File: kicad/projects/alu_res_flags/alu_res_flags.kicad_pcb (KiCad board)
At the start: 2 copper layers, 203.2 x 97.8 mm, 59 parts, among them J1 RES_CRRYBRRW_EQ_IN, J2 Aux_connection, J3 Bus_connection, J4 Control_signal_backplane, J5 ECNZ_OUT, U1 74HCT04, U10 74HCT245, U11 74HCT173, U12 74HCT245, U2 74HCT377, U3 74HCT377, U4 74HCT245, U5 74HCT245, U6 74HCT27, U7 74HCT27, U8 74HCT30, U9 74HCT245

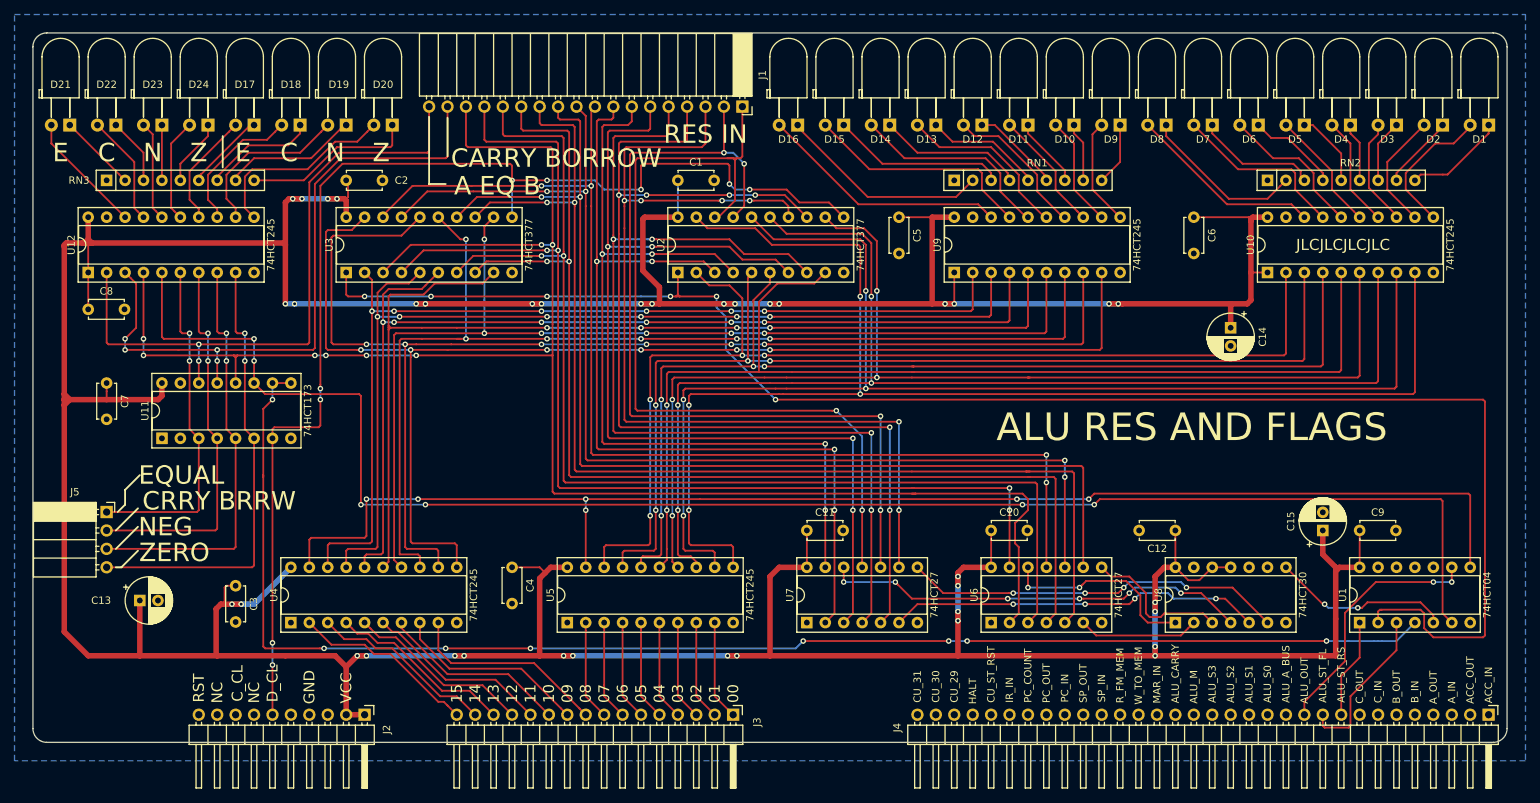
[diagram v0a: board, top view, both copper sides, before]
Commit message: Move kikad libs to sixteen bit location and update projects.
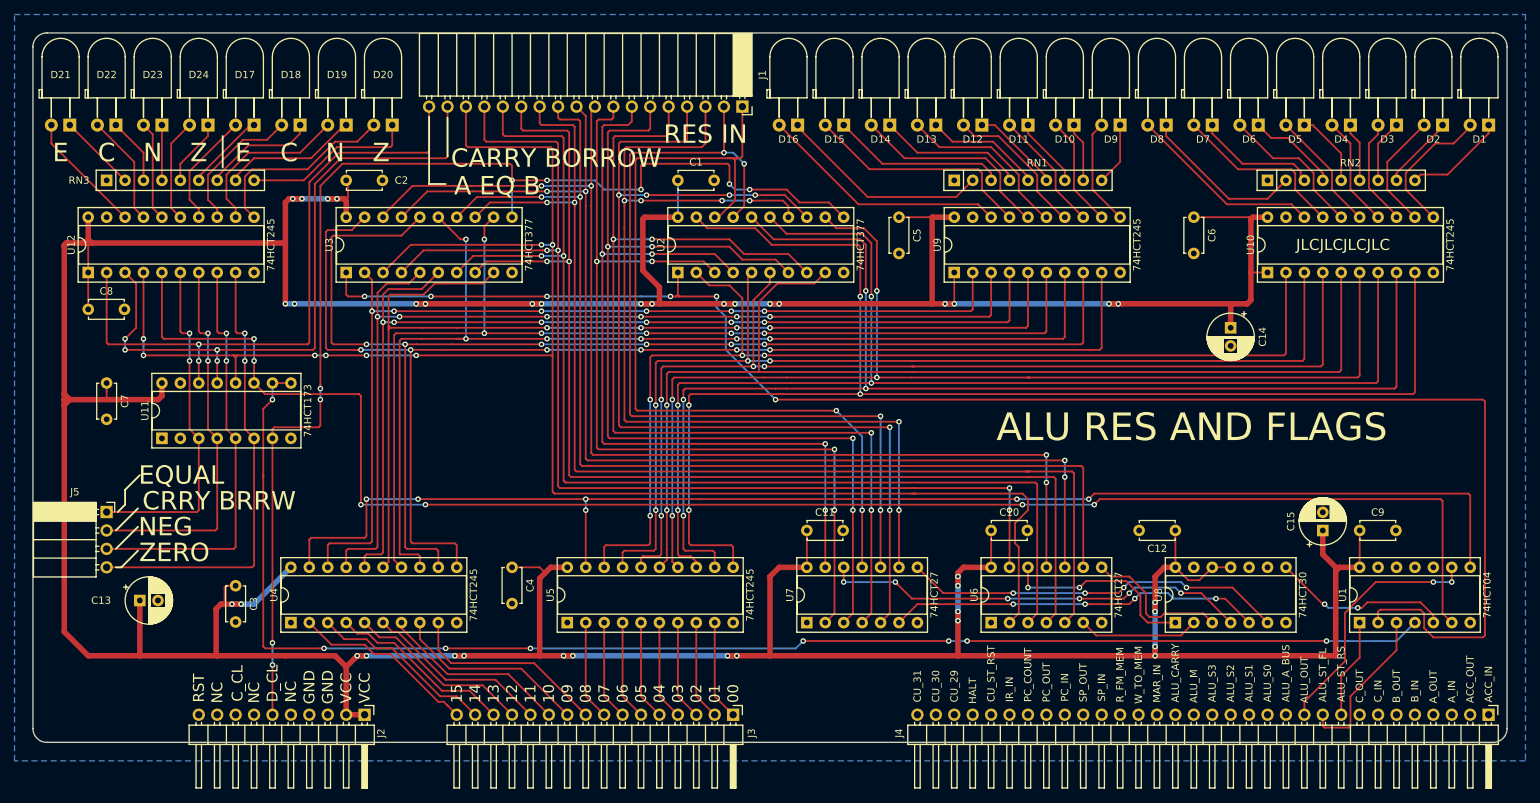
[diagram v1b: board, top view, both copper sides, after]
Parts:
- D1, D10, D11, D12, D13, D14, D15, D16, D17, D18, D19, D2, D20, D21, D22, D23, D24, D3, D4, D5, D6, D7, D8, D9: footprint eight-bit-computer:LED_D5.0mm_Horizontal_O3.81mm_Z3.0mm -> sixteen-bit-computer:LED_D5.0mm_Horizontal_O3.81mm_Z3.0mm
- J2: footprint eight-bit-computer:aux-connection -> sixteen-bit-computer:aux-connection
- J3: footprint eight-bit-computer:bus-connection -> sixteen-bit-computer:bus-connection
- J4: footprint eight-bit-computer:backplane-connector-single-row-annotated -> sixteen-bit-computer:backplane-connector-single-row-annotated

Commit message: Switch to HC series chips and fix some labelling in program counter or register PCB.
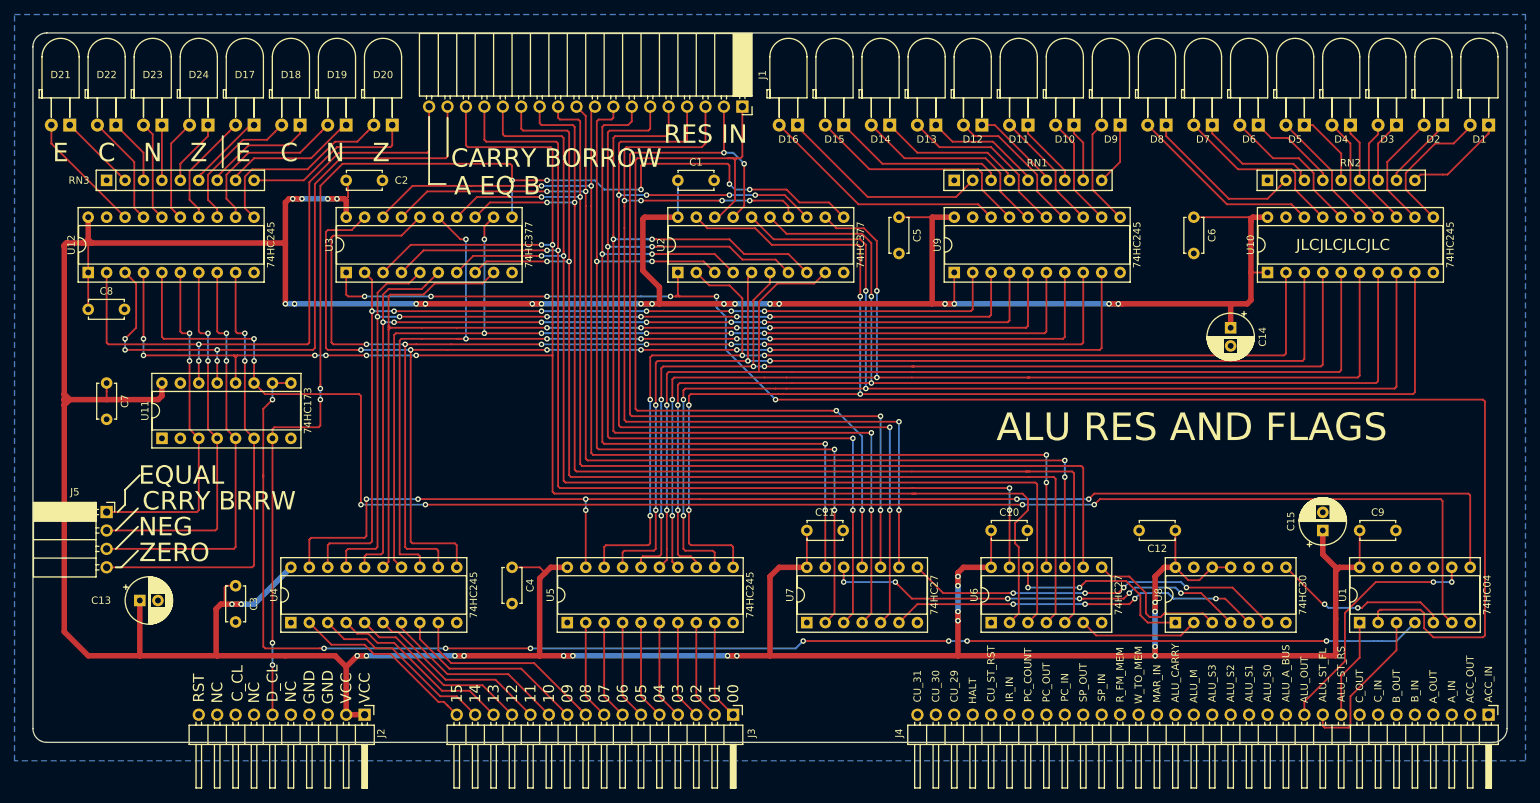
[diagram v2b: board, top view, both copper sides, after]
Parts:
- U1: value 74HCT04 -> 74HC04
- U10, U12, U4, U5, U9: value 74HCT245 -> 74HC245
- U11: value 74HCT173 -> 74HC173
- U2, U3: value 74HCT377 -> 74HC377
- U6, U7: value 74HCT27 -> 74HC27
- U8: value 74HCT30 -> 74HC30
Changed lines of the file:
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@@
       (effects (font (size 1.016 1.016) (thickness 0.1778)))
     )
-    (fp_text value 74HCT30 (at 3.81 17.57 90) (layer F.SilkS)
+    (fp_text value 74HC30 (at 3.81 17.57 90) (layer F.SilkS)
       (effects (font (size 1.016 1.016) (thickness 0.1778)))
     )
@@
       (effects (font (size 1.016 1.016) (thickness 0.1778)))
     )
-    (fp_text value 74HCT245 (at 3.81 25.19 90) (layer F.SilkS)
+    (fp_text value 74HC245 (at 3.81 25.19 90) (layer F.SilkS)
       (effects (font (size 1.016 1.016) (thickness 0.1778)))
     )
@@
       (effects (font (size 1.016 1.016) (thickness 0.1778)))
     )
-    (fp_text value 74HCT173 (at 3.81 20.11 90) (layer F.SilkS)
+    (fp_text value 74HC173 (at 3.81 20.11 90) (layer F.SilkS)
       (effects (font (size 1.016 1.016) (thickness 0.1778)))
     )
@@
       (effects (font (size 1.016 1.016) (thickness 0.1778)))
     )
-    (fp_text value 74HCT245 (at 3.81 25.19 90) (layer F.SilkS)
+    (fp_text value 74HC245 (at 3.81 25.19 90) (layer F.SilkS)
       (effects (font (size 1.016 1.016) (thickness 0.1778)))
     )
@@
       (effects (font (size 1.016 1.016) (thickness 0.1778)))
     )
-    (fp_text value 74HCT245 (at 3.81 25.19 90) (layer F.SilkS)
+    (fp_text value 74HC245 (at 3.81 25.19 90) (layer F.SilkS)
       (effects (font (size 1.016 1.016) (thickness 0.1778)))
     )
@@
       (effects (font (size 1.016 1.016) (thickness 0.1778)))
     )
-    (fp_text value 74HCT27 (at 3.81 17.57 90) (layer F.SilkS)
+    (fp_text value 74HC27 (at 3.81 17.57 90) (layer F.SilkS)
       (effects (font (size 1.016 1.016) (thickness 0.1778)))
     )
@@
       (effects (font (size 1.016 1.016) (thickness 0.1778)))
     )
-    (fp_text value 74HCT27 (at 3.81 17.57 90) (layer F.SilkS)
+    (fp_text value 74HC27 (at 3.81 17.57 90) (layer F.SilkS)
       (effects (font (size 1.016 1.016) (thickness 0.1778)))
     )
@@
       (effects (font (size 1.016 1.016) (thickness 0.1778)))
     )
-    (fp_text value 74HCT245 (at 3.81 25.19 90) (layer F.SilkS)
+    (fp_text value 74HC245 (at 3.81 25.19 90) (layer F.SilkS)
       (effects (font (size 1.016 1.016) (thickness 0.1778)))
     )
@@
       (effects (font (size 1.016 1.016) (thickness 0.1778)))
     )
-    (fp_text value 74HCT245 (at 3.81 25.19 90) (layer F.SilkS)
+    (fp_text value 74HC245 (at 3.81 25.19 90) (layer F.SilkS)
       (effects (font (size 1.016 1.016) (thickness 0.1778)))
     )
@@
       (effects (font (size 1.016 1.016) (thickness 0.1778)))
     )
-    (fp_text value 74HCT377 (at 3.81 25.19 90) (layer F.SilkS)
+    (fp_text value 74HC377 (at 3.81 25.19 90) (layer F.SilkS)
       (effects (font (size 1.016 1.016) (thickness 0.1778)))
     )
@@
       (effects (font (size 1.016 1.016) (thickness 0.1778)))
     )
-    (fp_text value 74HCT377 (at 3.81 25.19 90) (layer F.SilkS)
+    (fp_text value 74HC377 (at 3.81 25.19 90) (layer F.SilkS)
       (effects (font (size 1.016 1.016) (thickness 0.1778)))
     )
@@
       (effects (font (size 1.016 1.016) (thickness 0.1778)))
     )
-    (fp_text value 74HCT04 (at 3.81 17.57 90) (layer F.SilkS)
-      (effects (font (size 1.016 1.016) (thickness 0.1778)))
-    )
+    (fp_text value 74HC04 (at 3.81 17.57 90) (layer F.SilkS)
+      (effects (font (size 1.016 1.016) (thickness 0.1778)))
+    )

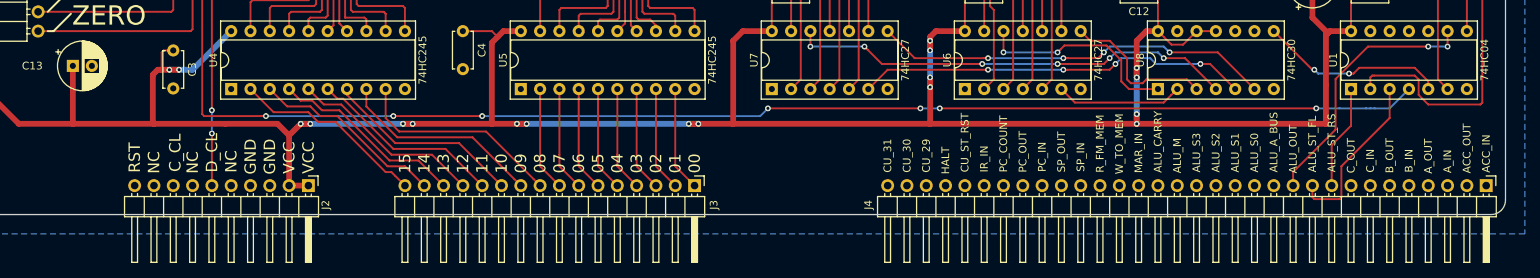
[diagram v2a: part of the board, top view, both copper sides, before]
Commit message: Move alu res flags lower connectors.
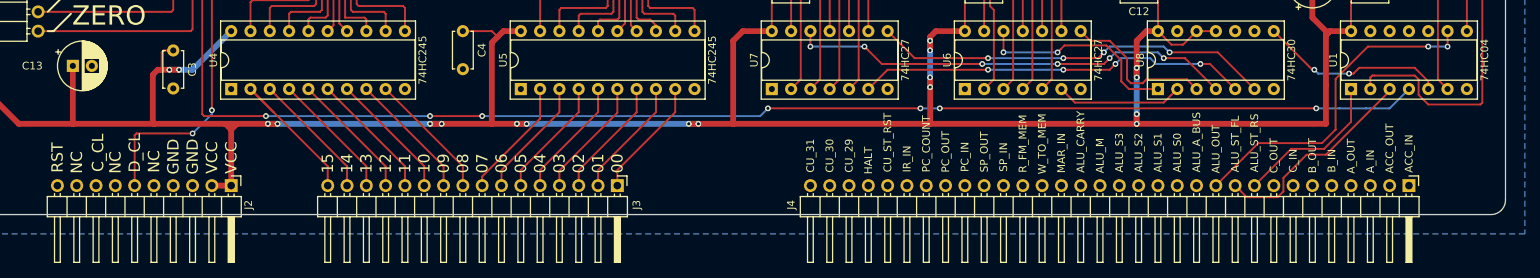
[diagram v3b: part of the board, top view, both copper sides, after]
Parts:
- moved J2 10.2 mm to (86.4, 149.9)
- moved J3 10.2 mm to (137.2, 149.9)
- moved J4 10.2 mm to (241.3, 149.9)
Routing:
- net /BUS_08: track 27.8 -> 16.9 mm
- net /BUS_09: track 26.9 -> 16.9 mm
- net /RES_OUT: track 34.9 -> 44.0 mm
- net /BUS_10: track 26.0 -> 16.9 mm
- net /BUS_14: track 25.6 -> 16.9 mm
- net /BUS_11: track 25.6 -> 16.9 mm
- net /BUS_13: track 25.6 -> 16.9 mm
- net /BUS_12: track 25.6 -> 16.9 mm
- net /CLOCK: track 168.3 -> 176.8 mm
- net /STORE_RES: track 13.8 -> 20.5 mm
- net /STORE_FLAGS: track 22.4 -> 28.0 mm
- net /BUS_15: track 25.6 -> 21.2 mm
- net VCC: track 713.0 -> 715.7 mm
- net /BUS_05: track 13.8 -> 15.9 mm
- net /BUS_07: track 13.8 -> 15.9 mm
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
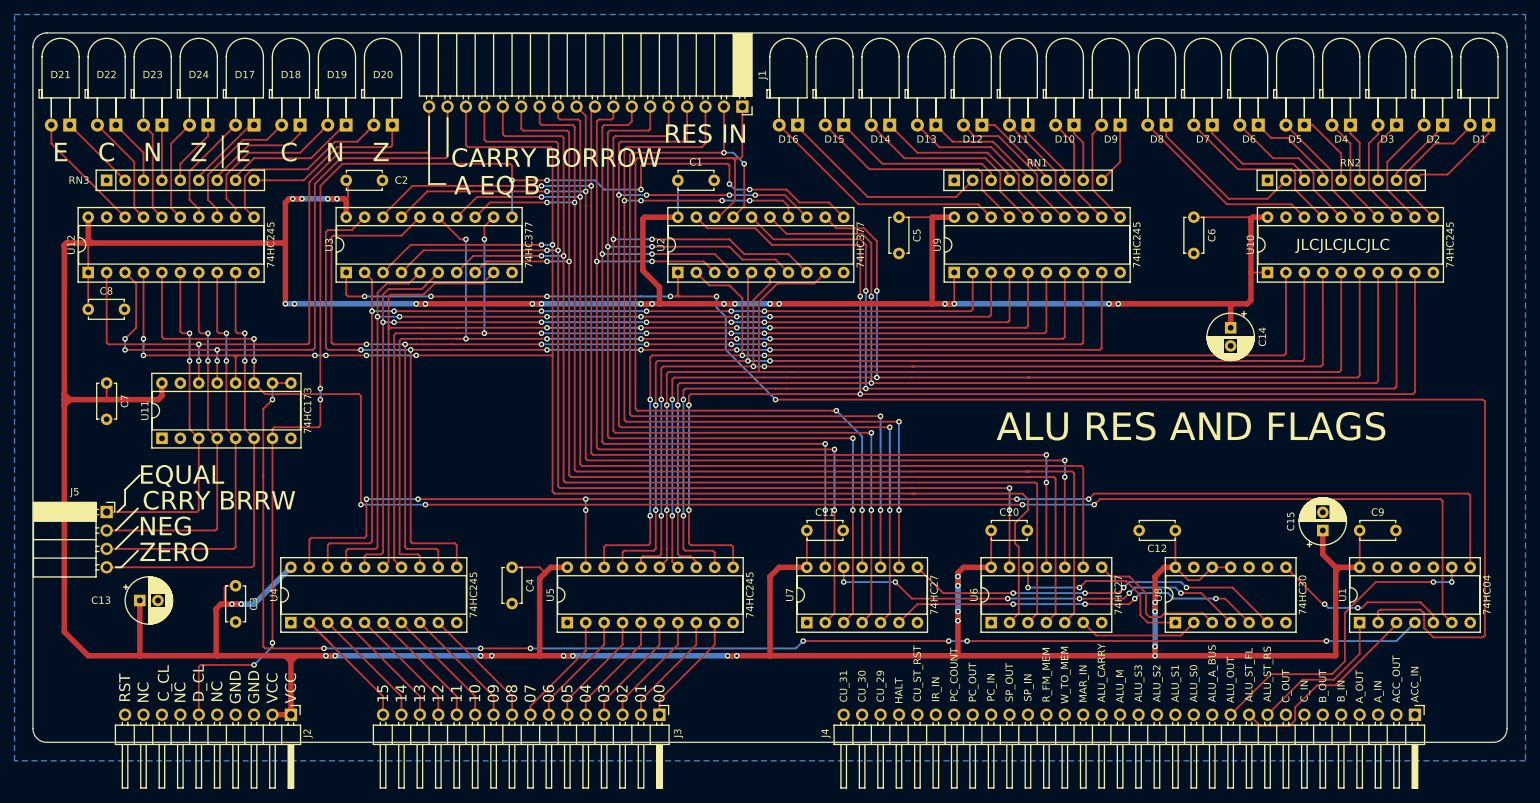
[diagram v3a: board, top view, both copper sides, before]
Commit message: Add LED control to ALU res flags.
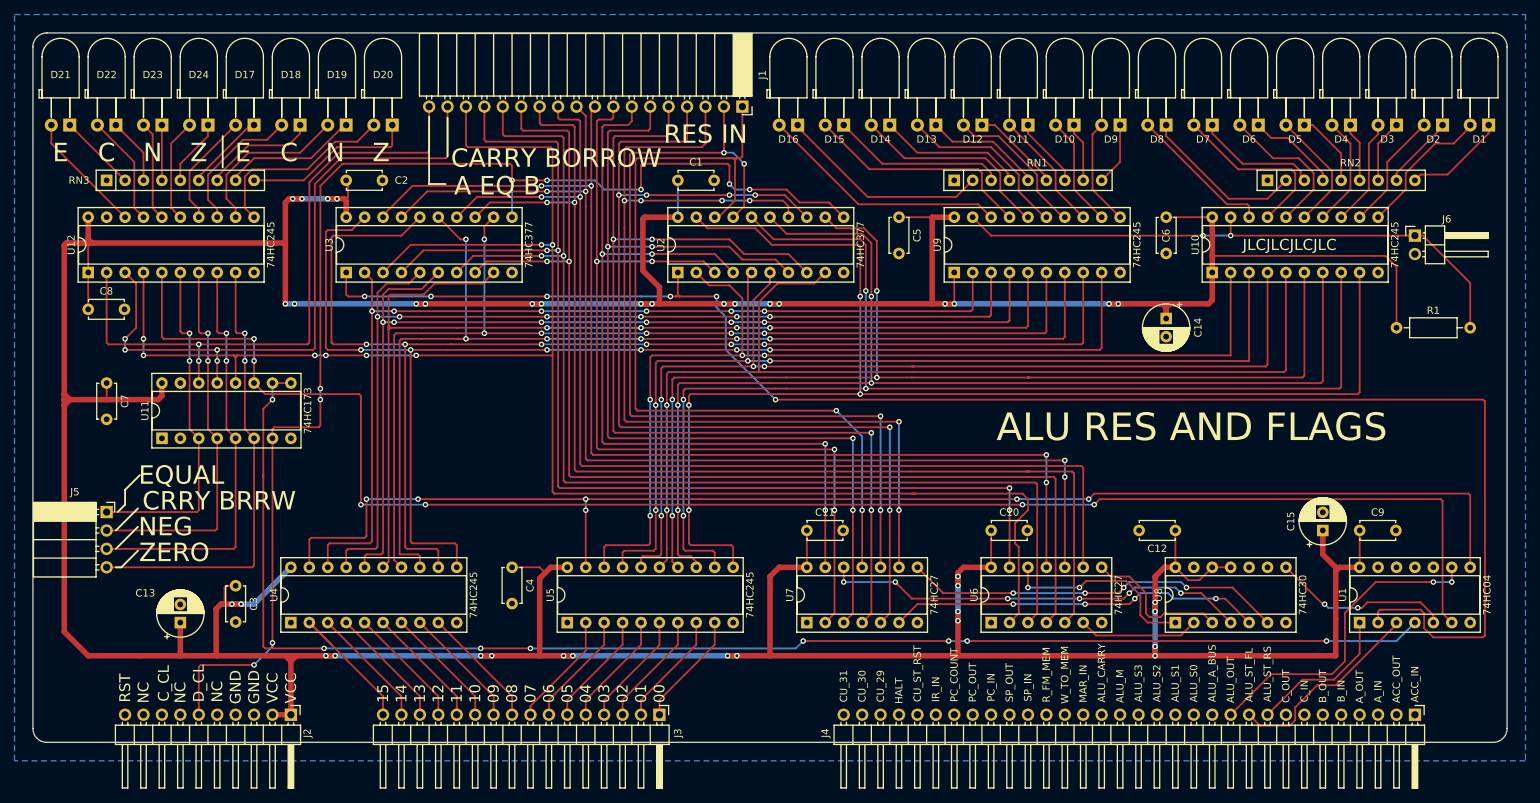
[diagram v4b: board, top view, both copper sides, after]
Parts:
- added J6: LED_CONTROL, Connector_PinHeader_2.54mm:PinHeader_1x02_P2.54mm_Horizontal, F.Cu at (241.3, 83.8)
- added R1: 10K, Resistor_THT:R_Axial_DIN0207_L6.3mm_D2.5mm_P10.16mm_Horizontal, F.Cu at (238.8, 96.5)
- moved C14 8.98 mm to (207.0, 95.2)
- moved U10 7.62 mm to (213.4, 88.9)
- moved C13 6.37 mm to (71.1, 137.2), turned to 90 degrees
- moved C6 3.81 mm to (207.0, 81.3)
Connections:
- U10 pad 19: GND -> /LED_CONTROL
- U9 pad 19: GND -> /LED_CONTROL
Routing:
- net /LED_CONTROL: track 0.00 -> 81.1 mm, vias 0 -> 2
- net VCC: track 715.7 -> 736.6 mm
- net /CLK_RES_05: track 148.2 -> 140.6 mm
- net /CLK_RES_03: track 162.9 -> 155.3 mm
- net /CLK_RES_02: track 173.6 -> 165.9 mm
- net /CLK_RES_01: track 179.8 -> 172.2 mm
- net /CLK_RES_00: track 190.8 -> 183.2 mm
- net /CLK_RES_04: track 154.7 -> 147.1 mm
- net /CLK_RES_07: track 149.7 -> 142.3 mm
- net /CLK_RES_06: track 146.7 -> 139.2 mm
- net Net-(D8-Pad2): track 26.9 -> 20.1 mm
